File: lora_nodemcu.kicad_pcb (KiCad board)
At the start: 4 copper layers, 25.8 x 32.9 mm, 17 parts, among them U1 RFM95, U2 LM1117-3.3, U3 WeMos_mini

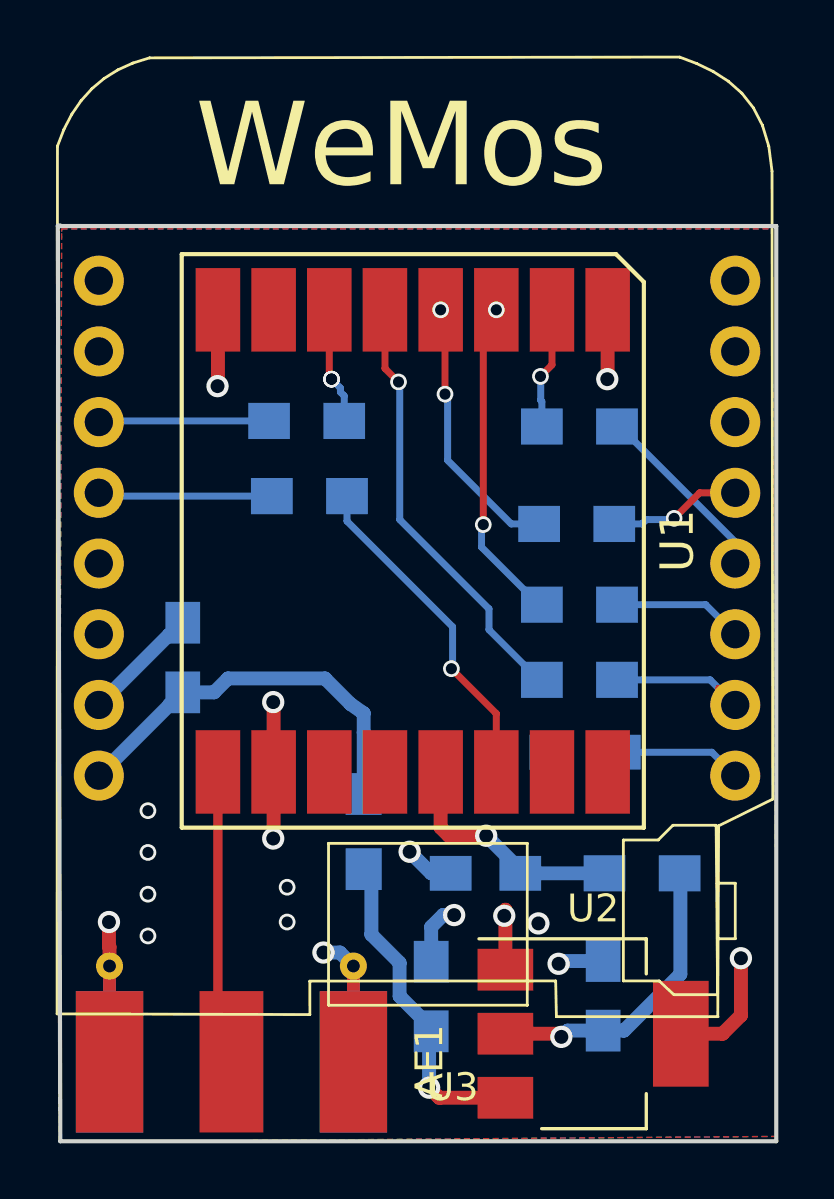
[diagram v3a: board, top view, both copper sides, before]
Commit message: really really removed Vias and moved a few traces
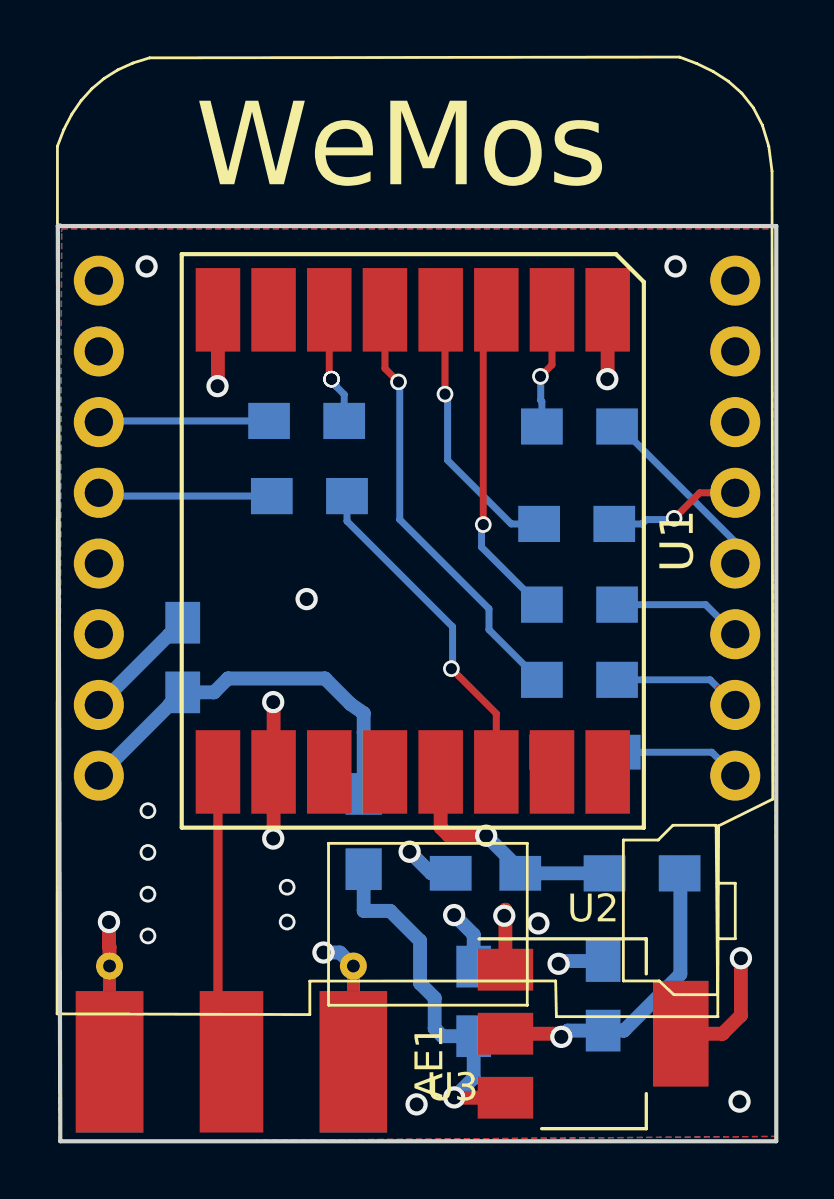
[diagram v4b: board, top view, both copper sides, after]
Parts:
- moved C1 1.54 mm to (150.7, 102.8)
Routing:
- net +5V: track 11.8 -> 13.2 mm
- net GND: track 31.6 -> 31.4 mm, vias 17 -> 22
- net Net-(R6-Pad2): vias 2 -> 1
- net Net-(R4-Pad2): vias 2 -> 1
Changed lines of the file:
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@@
     (thickness 1.2)
     (drawings 10)
-    (tracks 155)
+    (tracks 159)
     (zones 0)
     (modules 17)
@@
     (pad_to_mask_clearance 0.2)
     (aux_axis_origin 0 0)
-    (visible_elements FFFFFFFF)
+    (visible_elements FFFFFFDF)
     (pcbplotparams
-      (layerselection 0x010f0_80000007)
+      (layerselection 0x010f0_ffffffff)
       (usegerberextensions true)
       (usegerberattributes true)
@@
   )
   (module Capacitors_SMD:C_0805_HandSoldering (layer B.Cu)
-    (at 149.175 102.675 270)
+    (at 150.7 102.85 270)
     (descr "Capacitor SMD 0805, hand soldering")
     (tags "capacitor 0805")
@@
   (segment (start 137.2782 82) (end 137.2362 82.042) (width 0.25) (layer B.Cu) (net 3))
   (segment (start 143.308 82.042) (end 143.35 82) (width 0.25) (layer B.Cu) (net 3))
+  (segment (start 146.05 82) (end 146.05 81.05) (width 0.25) (layer B.Cu) (net 4))
+  (segment (start 146.05 81.05) (end 145.75 80.75) (width 0.25) (layer B.Cu) (net 4))
+  (segment (start 145.75 80.75) (end 145.75 80.655192) (width 0.25) (layer B.Cu) (net 4))
+  (segment (start 145.75 80.655192) (end 145.594409 80.499601) (width 0.25) (layer B.Cu) (net 4))
   (segment (start 145.5138 78.0092) (end 145.5138 80.418992) (width 0.25) (layer F.Cu) (net 4))
   (segment (start 145.5138 80.418992) (end 145.594409 80.499601) (width 0.25) (layer F.Cu) (net 4))
   (via (at 145.594409 80.499601) (size 0.6) (drill 0.4) (layers F.Cu B.Cu) (net 4))
-  (segment (start 145.914184 80.964184) (end 145.914184 80.819376) (width 0.25) (layer B.Cu) (net 4))
-  (segment (start 145.914184 80.819376) (end 145.594409 80.499601) (width 0.25) (layer B.Cu) (net 4))
   (via (at 145.594409 80.499601) (size 0.6) (drill 0.4) (layers F.Cu B.Cu) (net 4))
-  (segment (start 146.05 82) (end 146.05 81.1) (width 0.25) (layer B.Cu) (net 4))
-  (segment (start 146.05 81.1) (end 145.914184 80.964184) (width 0.25) (layer B.Cu) (net 4))
   (segment (start 155.85 91.3) (end 159.1942 91.3) (width 0.25) (layer B.Cu) (net 5))
   (segment (start 159.1942 91.3) (end 160.0962 92.202) (width 0.25) (layer B.Cu) (net 5))
@@
   (segment (start 149.670978 81.036697) (end 149.670978 78.166378) (width 0.25) (layer F.Cu) (net 8))
   (segment (start 149.670978 78.166378) (end 149.5138 78.0092) (width 0.25) (layer F.Cu) (net 8))
-  (via (at 149.5138 78.0092) (size 0.6) (drill 0.4) (layers F.Cu B.Cu) (net 8))
   (segment (start 149.764715 83.414715) (end 149.764715 81.130434) (width 0.25) (layer B.Cu) (net 8))
   (segment (start 149.764715 81.130434) (end 149.670978 81.036697) (width 0.25) (layer B.Cu) (net 8))
@@
   (segment (start 151.045786 85.723543) (end 151.045786 78.477214) (width 0.25) (layer F.Cu) (net 12))
   (segment (start 151.045786 78.477214) (end 151.5138 78.0092) (width 0.25) (layer F.Cu) (net 12))
-  (via (at 151.5138 78.0092) (size 0.6) (drill 0.4) (layers F.Cu B.Cu) (net 12))
   (segment (start 150.983295 86.533295) (end 150.983295 85.786034) (width 0.25) (layer B.Cu) (net 12))
   (segment (start 150.983295 85.786034) (end 151.045786 85.723543) (width 0.25) (layer B.Cu) (net 12))
@@
   (segment (start 153.15 88.6) (end 153.05 88.6) (width 0.25) (layer B.Cu) (net 12))
   (segment (start 153.05 88.6) (end 150.983295 86.533295) (width 0.25) (layer B.Cu) (net 12))
+  (via (at 144.7 88.4) (size 0.8) (drill 0.5) (layers F.Cu B.Cu) (net 14))
+  (via (at 138.95 76.45) (size 0.8) (drill 0.5) (layers F.Cu B.Cu) (net 14))
+  (via (at 157.95 76.45) (size 0.8) (drill 0.5) (layers F.Cu B.Cu) (net 14))
+  (via (at 160.25 106.45) (size 0.8) (drill 0.5) (layers F.Cu B.Cu) (net 14))
+  (via (at 148.65 106.55) (size 0.8) (drill 0.5) (layers F.Cu B.Cu) (net 14))
+  (segment (start 150.7 101.6) (end 150.7 100.45) (width 0.5) (layer B.Cu) (net 14))
+  (segment (start 150.7 100.45) (end 150 99.75) (width 0.5) (layer B.Cu) (net 14))
+  (via (at 150 99.75) (size 0.8) (drill 0.5) (layers F.Cu B.Cu) (net 14))
   (segment (start 143.5138 94.6092) (end 143.5138 92.1138) (width 0.5) (layer F.Cu) (net 14))
   (segment (start 143.5138 92.1138) (end 143.5 92.1) (width 0.5) (layer F.Cu) (net 14))
@@
   (segment (start 139.775 89.675) (end 139.7632 89.675) (width 0.5) (layer B.Cu) (net 14))
   (segment (start 139.7632 89.675) (end 137.2362 92.202) (width 0.5) (layer B.Cu) (net 14))
-  (segment (start 149.175 100.175) (end 149.6 99.75) (width 0.5) (layer B.Cu) (net 14))
-  (segment (start 149.6 99.75) (end 150 99.75) (width 0.5) (layer B.Cu) (net 14))
-  (segment (start 149.175 101.425) (end 149.175 100.175) (width 0.5) (layer B.Cu) (net 14))
-  (via (at 150 99.75) (size 0.8) (drill 0.5) (layers F.Cu B.Cu) (net 14))
   (segment (start 151.8408 99.5592) (end 151.8408 99.7342) (width 0.5) (layer F.Cu) (net 14))
   (segment (start 151.8408 99.7342) (end 151.8 99.775) (width 0.5) (layer F.Cu) (net 14))
@@
   (segment (start 158.1408 104.013) (end 159.6408 104.013) (width 0.5) (layer F.Cu) (net 16))
   (segment (start 159.6408 104.013) (end 160.3 103.3538) (width 0.5) (layer F.Cu) (net 16))
-  (segment (start 148.040001 102.665001) (end 148.040001 101.465001) (width 0.5) (layer B.Cu) (net 20))
-  (segment (start 148.040001 101.465001) (end 147.025 100.45) (width 0.5) (layer B.Cu) (net 20))
-  (segment (start 149.175 103.8) (end 148.040001 102.665001) (width 0.5) (layer B.Cu) (net 20))
-  (segment (start 149.175 103.925) (end 149.175 103.8) (width 0.5) (layer B.Cu) (net 20))
-  (segment (start 147.025 100.45) (end 147.025 98.375) (width 0.5) (layer B.Cu) (net 20))
-  (segment (start 147.025 98.375) (end 146.75 98.1) (width 0.5) (layer B.Cu) (net 20))
-  (segment (start 149.1 105.95) (end 149.1 104) (width 0.5) (layer B.Cu) (net 20))
-  (segment (start 149.1 104) (end 149.175 103.925) (width 0.5) (layer B.Cu) (net 20))
-  (segment (start 151.8408 106.313) (end 149.463 106.313) (width 0.5) (layer F.Cu) (net 20))
-  (segment (start 149.463 106.313) (end 149.1 105.95) (width 0.5) (layer F.Cu) (net 20))
-  (via (at 149.1 105.95) (size 0.8) (drill 0.5) (layers F.Cu B.Cu) (net 20))
+  (segment (start 149.3 103.825) (end 149.3 102.725) (width 0.5) (layer B.Cu) (net 20))
+  (segment (start 149.575 104.1) (end 149.3 103.825) (width 0.5) (layer B.Cu) (net 20))
+  (segment (start 149.3 102.725) (end 148.775 102.2) (width 0.5) (layer B.Cu) (net 20))
+  (segment (start 150.7 104.1) (end 149.575 104.1) (width 0.5) (layer B.Cu) (net 20))
+  (segment (start 148.775 102.2) (end 148.775 100.675) (width 0.5) (layer B.Cu) (net 20))
+  (segment (start 148.775 100.675) (end 147.7 99.6) (width 0.5) (layer B.Cu) (net 20))
+  (segment (start 147.7 99.6) (end 146.75 99.6) (width 0.5) (layer B.Cu) (net 20))
+  (segment (start 146.75 99.6) (end 146.75 98.1) (width 0.5) (layer B.Cu) (net 20))
+  (segment (start 150.7 104.1) (end 150.7 105.6) (width 0.5) (layer B.Cu) (net 20))
+  (segment (start 150.7 105.6) (end 150 106.3) (width 0.5) (layer B.Cu) (net 20))
+  (segment (start 151.8408 106.313) (end 150.013 106.313) (width 0.5) (layer F.Cu) (net 20))
+  (segment (start 150.013 106.313) (end 150 106.3) (width 0.5) (layer F.Cu) (net 20))
+  (via (at 150 106.3) (size 0.8) (drill 0.5) (layers F.Cu B.Cu) (net 20))
   (segment (start 141.5138 94.6092) (end 141.5138 104.5338) (width 0.335589) (layer F.Cu) (net 28))
   (segment (start 141.5138 104.5338) (end 142 105.02) (width 0.25) (layer F.Cu) (net 28))

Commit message: added ground plane keepout bellow SMA connector
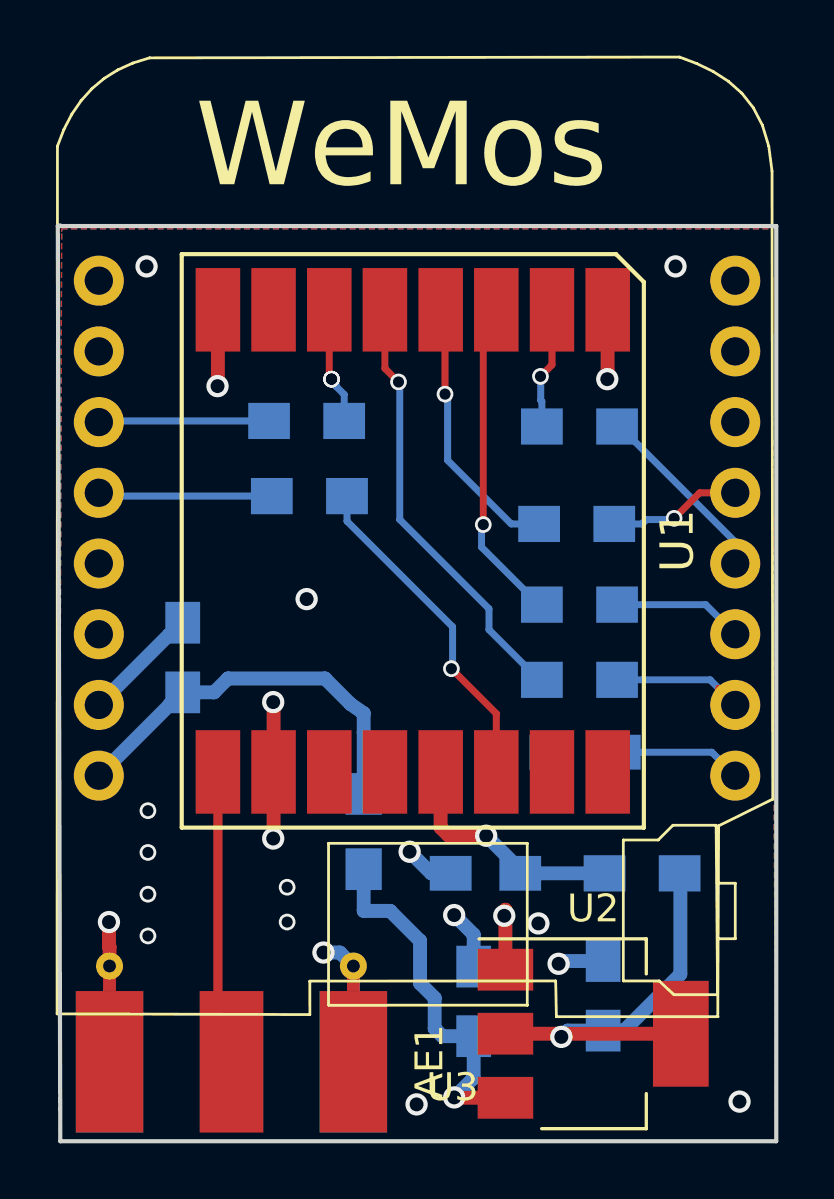
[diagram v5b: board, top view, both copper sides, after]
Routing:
- net +3V3: track 14.8 -> 14.6 mm, vias 2 -> 1
- added copper zone on In2.Cu, net GND
- removed copper zone on In2.Cu, net +3V3
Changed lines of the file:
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@@
     (thickness 1.2)
     (drawings 10)
-    (tracks 159)
+    (tracks 157)
     (zones 0)
     (modules 17)
@@
   (segment (start 137.62 101.58) (end 137.62 100.894107) (width 0.5) (layer F.Cu) (net 14))
   (segment (start 137.62 100.894107) (end 137.6 100.874107) (width 0.5) (layer F.Cu) (net 14))
+  (segment (start 158.1408 104.013) (end 153.962 104.013) (width 0.5) (layer F.Cu) (net 16))
+  (segment (start 153.962 104.013) (end 153.85 104.125) (width 0.5) (layer F.Cu) (net 16))
   (segment (start 155.35 103.9) (end 154.075 103.9) (width 0.5) (layer B.Cu) (net 16))
   (segment (start 154.075 103.9) (end 153.85 104.125) (width 0.5) (layer B.Cu) (net 16))
@@
   (via (at 153.85 104.125) (size 0.8) (drill 0.5) (layers F.Cu B.Cu) (net 16))
   (segment (start 153.738 104.013) (end 153.85 104.125) (width 0.5) (layer F.Cu) (net 16))
-  (via (at 160.3 101.3) (size 0.8) (drill 0.5) (layers F.Cu B.Cu) (net 16))
-  (segment (start 160.3 103.3538) (end 160.3 101.3) (width 0.5) (layer F.Cu) (net 16))
-  (segment (start 158.1408 104.013) (end 159.6408 104.013) (width 0.5) (layer F.Cu) (net 16))
-  (segment (start 159.6408 104.013) (end 160.3 103.3538) (width 0.5) (layer F.Cu) (net 16))
   (segment (start 149.3 103.825) (end 149.3 102.725) (width 0.5) (layer B.Cu) (net 20))
   (segment (start 149.575 104.1) (end 149.3 103.825) (width 0.5) (layer B.Cu) (net 20))
@@
     (polygon
       (pts
-        (xy 135.9 75.1) (xy 161.4 75.1) (xy 161.6 107.7) (xy 135.8 107.9) (xy 135.9 75.2)
+        (xy 135.9 75.1) (xy 161.4 75.1) (xy 161.55 107.9) (xy 135.8 107.9) (xy 135.9 75.2)
       )
     )
@@
     (polygon
       (pts
-        (xy 135.9 75.2) (xy 161.5 75.2) (xy 161.4 107.9) (xy 135.8 107.8) (xy 135.8 75.1)
+        (xy 135.9 75.2) (xy 161.5 75.2) (xy 161.55 107.9) (xy 135.8 107.8) (xy 135.8 75.1)
       )
     )
   )
-  (zone (net 16) (net_name +3V3) (layer In2.Cu) (hatch edge 0.508)
+  (zone (net 14) (net_name GND) (layer In2.Cu) (hatch edge 0.508)
     (connect_pads (clearance 0.1524))
     (min_thickness 0.254)
@@
     (polygon
       (pts
-        (xy 135.9 75.1) (xy 161.4 75.1) (xy 161.6 107.7) (xy 135.8 107.9) (xy 135.9 75.2)
+        (xy 135.9 75.1) (xy 161.4 75.1) (xy 161.6 107.85) (xy 135.8 107.9) (xy 135.9 75.2)
       )
     )
@@
     (polygon
       (pts
-        (xy 135.9 75.1) (xy 161.4 75.1) (xy 161.6 107.7) (xy 135.8 107.9) (xy 135.9 75.2)
+        (xy 135.9 75.1) (xy 161.4 75.1) (xy 161.55 107.9) (xy 135.8 107.9) (xy 135.9 75.2)
       )
     )
+  )
+  (zone (net 0) (net_name "") (layers F.Cu In1.Cu) (hatch edge 0.508)
+    (connect_pads (clearance 0.1524))
+    (min_thickness 0.254)
+    (keepout (tracks allowed) (vias allowed) (copperpour not_allowed))
+    (fill (arc_segments 16) (thermal_gap 0.508) (thermal_bridge_width 0.508))
+    (polygon
+      (pts
+        (xy 139 107.9) (xy 139 102.3) (xy 145.2 102.3) (xy 145.2 107.85)
+      )
+    )

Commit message: modified top silkscreen
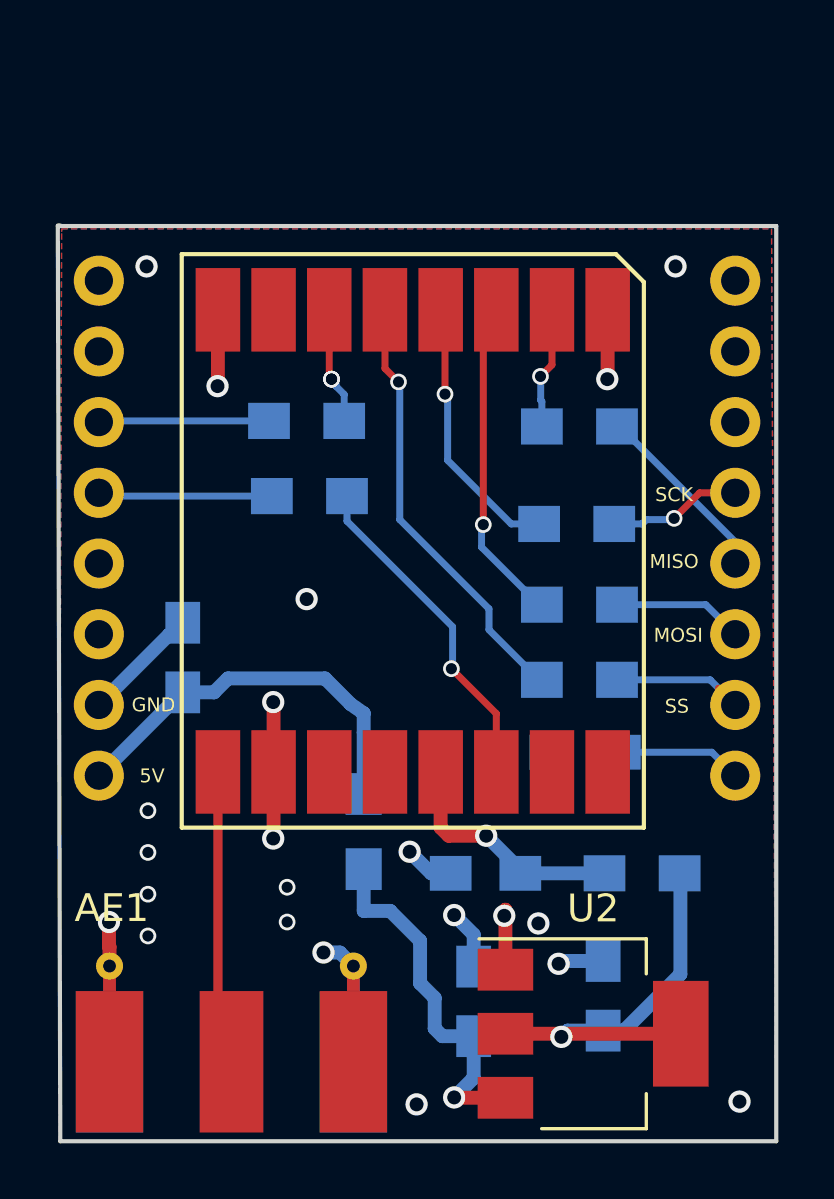
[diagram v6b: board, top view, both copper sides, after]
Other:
- board text added: "5V"
- board text added: "GND"
- board text added: "MISO"
- board text added: "MOSI"
- board text added: "SCK"
- board text added: "SS"
